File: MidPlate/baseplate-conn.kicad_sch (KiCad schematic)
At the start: 5 parts, among them J13 JST_BM04B-GHS-TBT, J3 JST_B3B-XH-A, J7 1586842-6

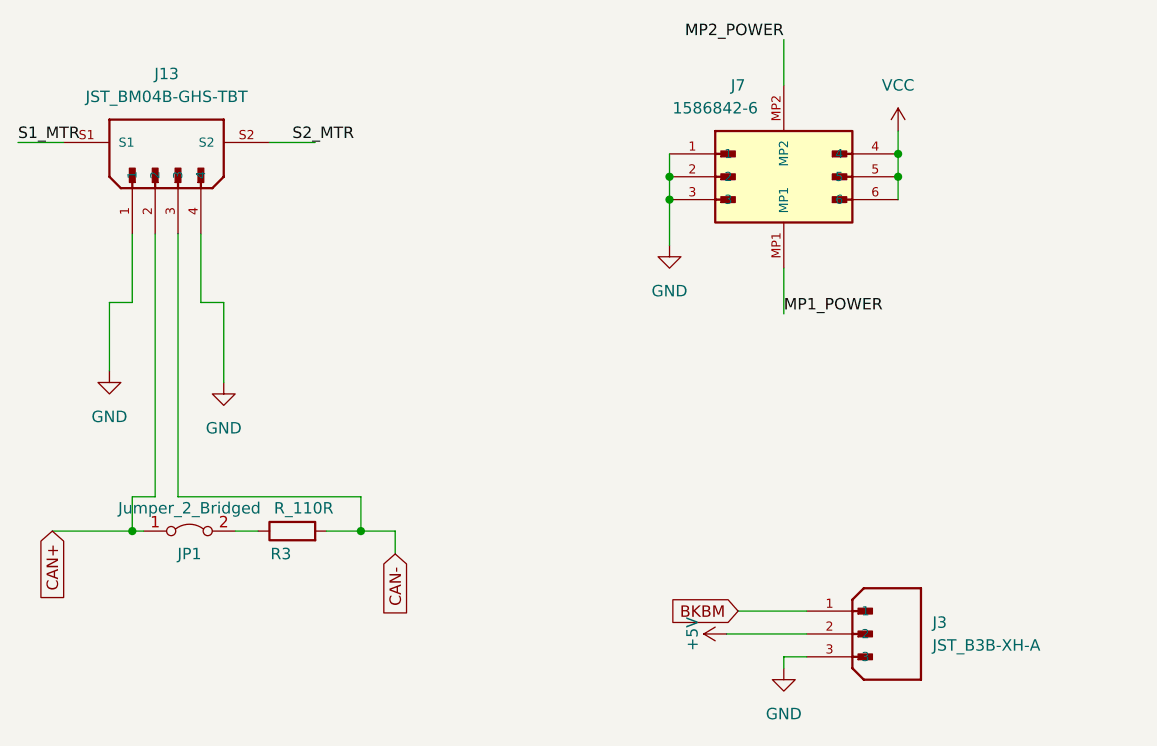
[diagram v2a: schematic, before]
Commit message: midplate updates
- pretty close to order: need to verify if we can get 2oz outer copper
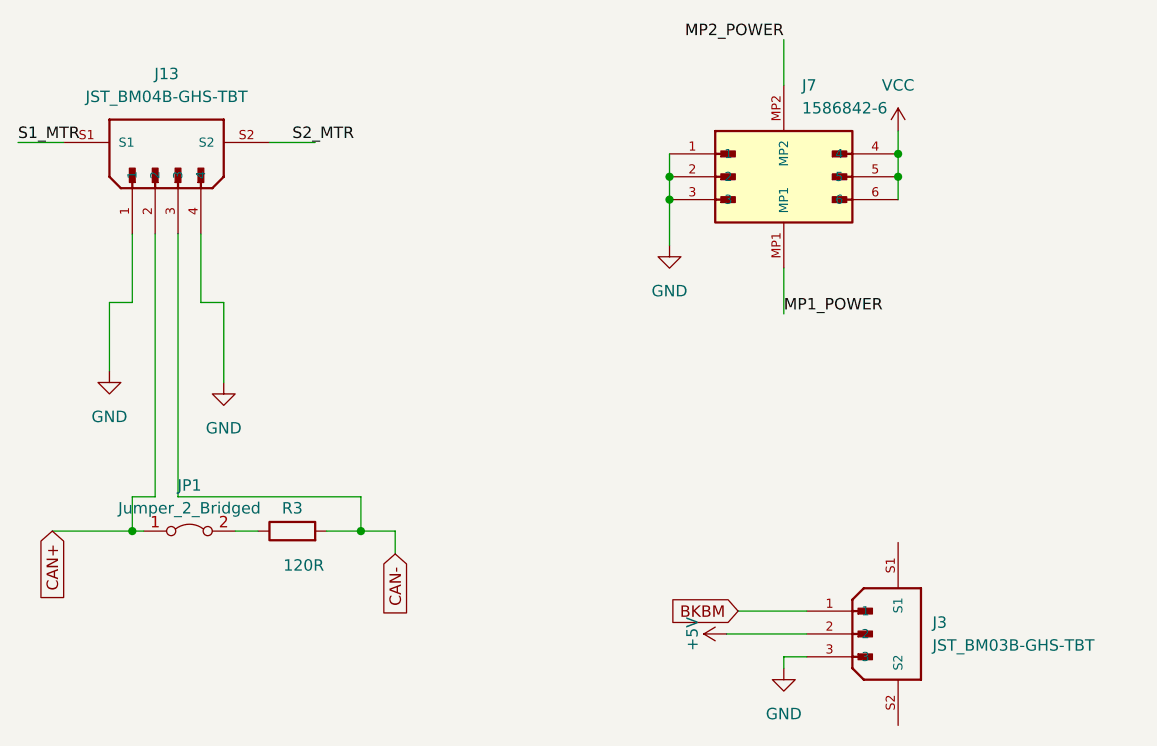
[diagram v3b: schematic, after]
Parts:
- removed J3: JST_B3B-XH-A, bots:JST_B3B-XH-A, symbol bots:JST_B3B-XH-A
- removed J7: 1586842-6, bots:TE_1586842-6_6PIN, symbol bots:TE_1586842-6_6PIN
- removed JP1: Jumper_2_Bridged, Connector_PinHeader_2.54mm:PinHeader_1x02_P2.54mm_Vertical, symbol Jumper:Jumper_2_Bridged
- removed R3: R_110R, bots:R_0603_1608Metric, symbol bots:R_110R
- added J3: JST_BM03B-GHS-TBT, bots:JST_BM03B-GHS-TBT, symbol thebots_symlib:JST_BM03B-GHS-TBT
- added J7: 1586842-6, bots:TE_1586842-6_6PIN, symbol thebots_symlib:TE_1586842-6_6PIN
- added JP1: Jumper_2_Bridged, Connector_PinHeader_2.54mm:PinHeader_1x02_P2.54mm_Vertical, symbol thebots_symlib:Jumper_2_Bridged
- added R3: 120R, bots:R_0603_1608Metric, symbol thebots_symlib:R_120R
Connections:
- net +5V: now also J3.2
- net BKBM: now also J3.1
- net CAN+: now also JP1.1 (A)
- net CAN-: now also R3.2
- net GND: now also J3.3, J7.1, J7.2, J7.3
- net MP1_POWER: now also J7.MP1
- net MP2_POWER: now also J7.MP2
- net VCC: now also J7.4, J7.5, J7.6
- new net: JP1.2 (B), R3.1

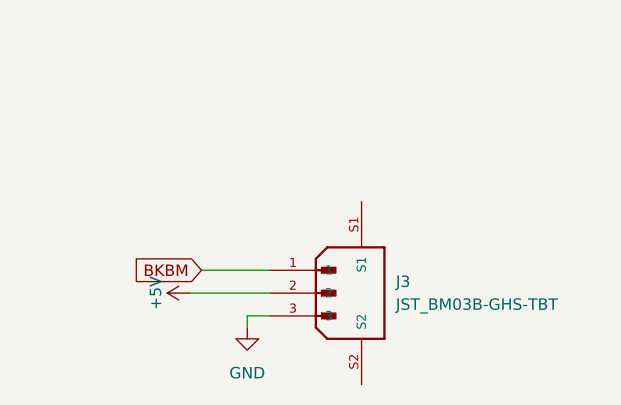
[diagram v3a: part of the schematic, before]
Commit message: chicker + midplate changes
-ready to order midplate
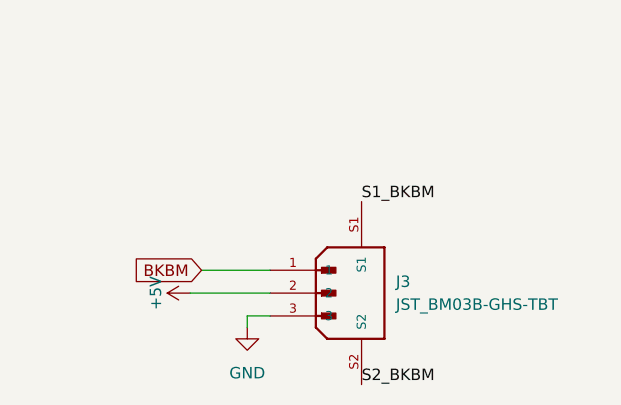
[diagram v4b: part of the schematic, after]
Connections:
- net S1_BKBM: now reaches J3.S1
- net S2_BKBM: now reaches J3.S2
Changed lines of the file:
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@@
     (stroke (width 0) (type default))
+  )
+  (label "S2_BKBM" (at 195.58 127 0) (fields_autoplaced)
+    (effects (font (size 1.27 1.27)) (justify left bottom))
   )
   (label "S2_MTR" (at 128.27 62.23 0) (fields_autoplaced)
@@
     (effects (font (size 1.27 1.27)) (justify right bottom))
   )
+  (label "S1_BKBM" (at 195.58 106.68 0) (fields_autoplaced)
+    (effects (font (size 1.27 1.27)) (justify left bottom))
+  )
   (label "S1_MTR" (at 97.79 62.23 0) (fields_autoplaced)

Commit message: some components files not working. checking a previous midplate branch
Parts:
- J13: symbol thebots_symlib:JST_BM04B-GHS-TBT -> bots:JST_BM04B-GHS-TBT
- J3: symbol thebots_symlib:JST_BM03B-GHS-TBT -> bots:JST_BM03B-GHS-TBT
- J7: symbol thebots_symlib:TE_1586842-6_6PIN -> bots:TE_1586842-6_6PIN
- JP1: symbol thebots_symlib:Jumper_2_Bridged -> bots:Jumper_2_Bridged
- R3: symbol thebots_symlib:R_120R -> bots:R_120R

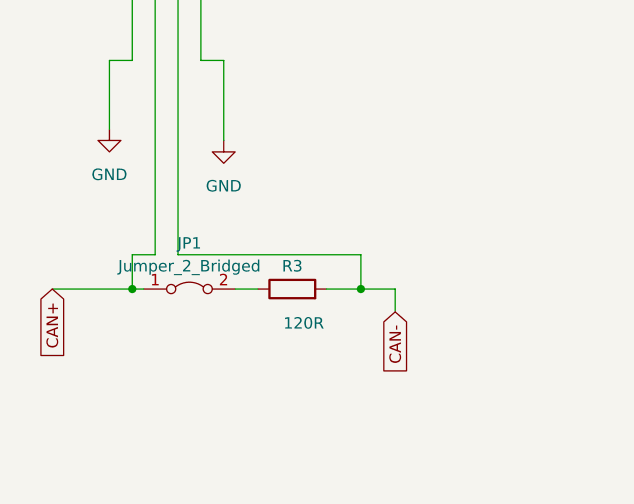
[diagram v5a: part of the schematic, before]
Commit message: midplate pass through
ethernet pass through
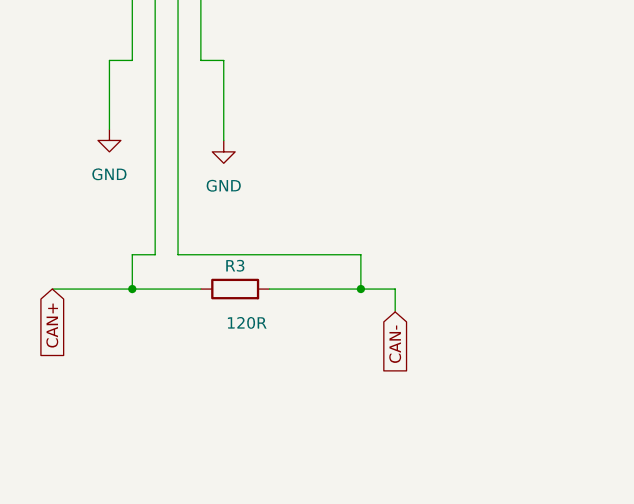
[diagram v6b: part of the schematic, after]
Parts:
- removed JP1: Jumper_2_Bridged, Connector_PinHeader_2.54mm:PinHeader_1x02_P2.54mm_Vertical, symbol bots:Jumper_2_Bridged
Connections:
- net CAN+: now also R3.1
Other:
- moved on the sheet: R3
